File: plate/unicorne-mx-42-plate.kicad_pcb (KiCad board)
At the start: 2 copper layers, 293.4 x 118.8 mm, 10 parts

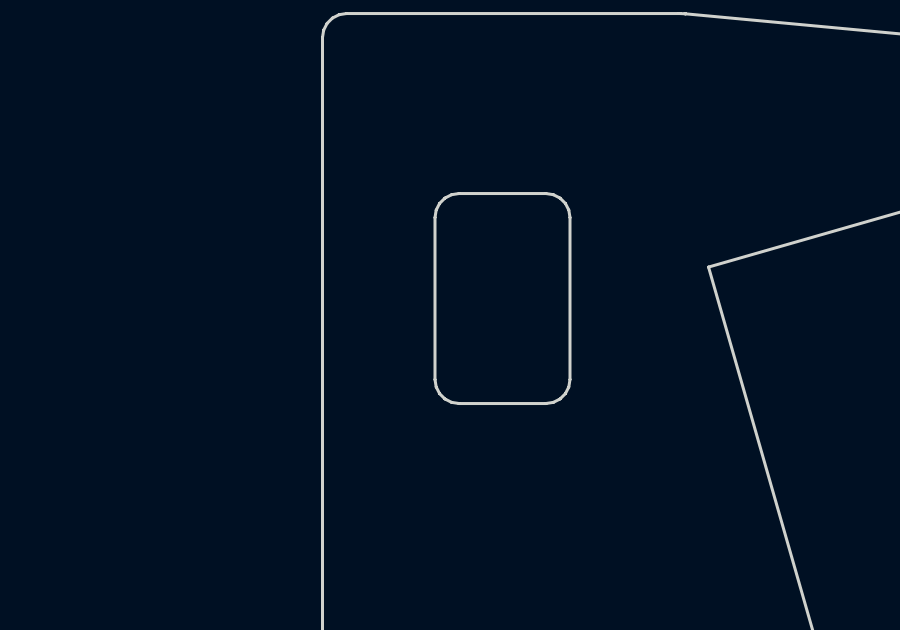
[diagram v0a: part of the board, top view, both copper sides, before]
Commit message: Route both boards with KiCadRoutingTools; no vias in pads
tools/krt_route.py: fixed lanes, then KiCadRoutingTools 0.23.7 for every other
signal at standard JLCPCB sizes (0.6/0.3 vias, 0.2 tracks) with no via in or next
to a pad, own net's included; the maze router for any net it could only finish
with undersized vias; GND pours and stitching; its plane repair; then any via
touching a pad is removed. The tools relax the project's rules on disk: ours are
put back.

MX lanes: LED_VDD's jog across a break line moves from 5.5 to 4.5 mm off the
line. At 5.5 it boxed in the outer-column LED DIN pads, so 8 LED data links had
no room for a via outside a pad. Lane-only board: no DRC errors.

Stitching vias (finish_route.stitch) and our maze router stay off SMD pads too.
The previous MX board had 82 vias in pads, now none on either board.

MX: U2 pad 3 (GND) is boxed in by LED_DIN; joined by hand with a via between
pads 3 and 4 (noted in the README).

Both boards: DRC 0 unconnected, 0 copper violations, schematic parity clean;
all 482 schematic pins, 42 keys and the 54-LED chain check out pin by pin.
Waves, LED map, plates, gerbers, STEP and renders regenerated.

Co-Authored-By: Claude Opus 5.5 <noreply@anthropic.com>
Claude-Session: https://claude.ai/code/session_01D39ubfTYtq6FMvNmmbStTo
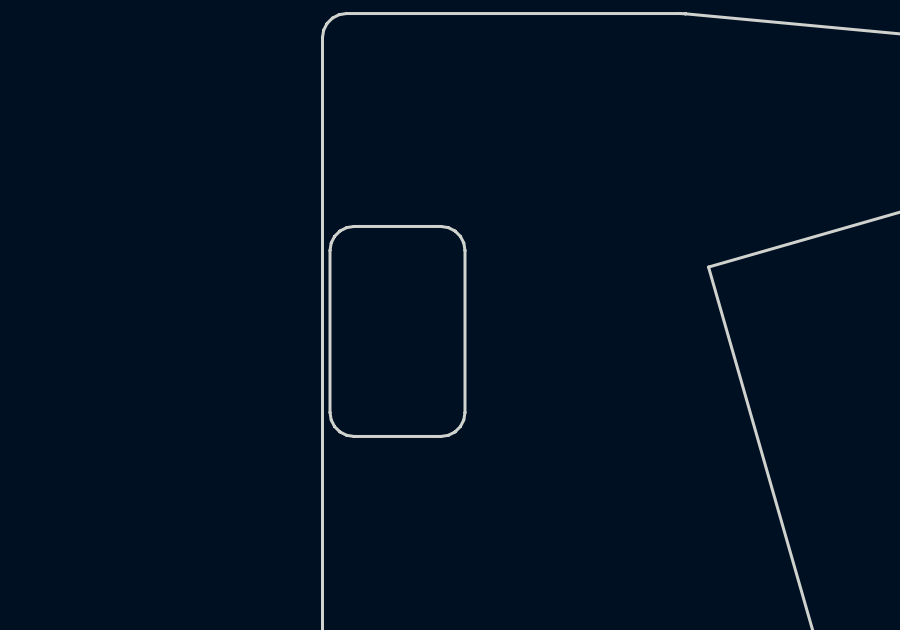
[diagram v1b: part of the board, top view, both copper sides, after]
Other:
- outline, holes or cut-outs redrawn
